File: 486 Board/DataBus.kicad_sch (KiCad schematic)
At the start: 16 parts, among them U21 74245, U22 74245, U23 74245, U24 74245, U25 74245, U26 74245, U27 74245, U28 74245

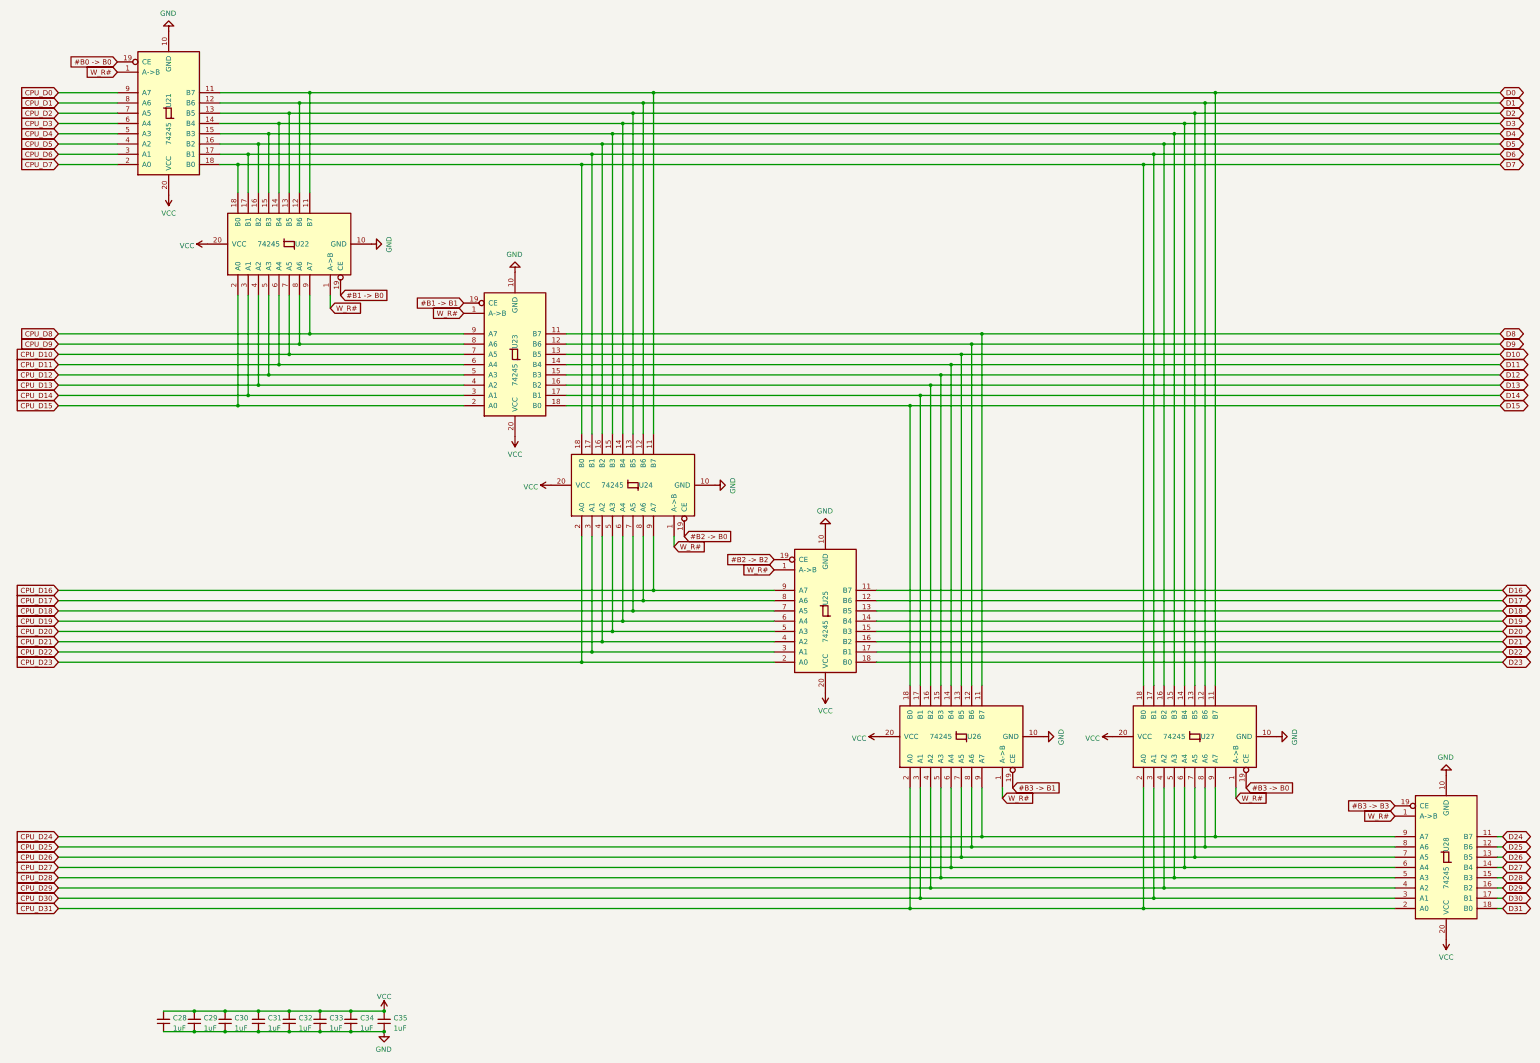
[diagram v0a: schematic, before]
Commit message: * Layout Template for eurocard format * 486 Board updated to new layout * Support board draft * Added 6u eurocard backplane meant for ATX case
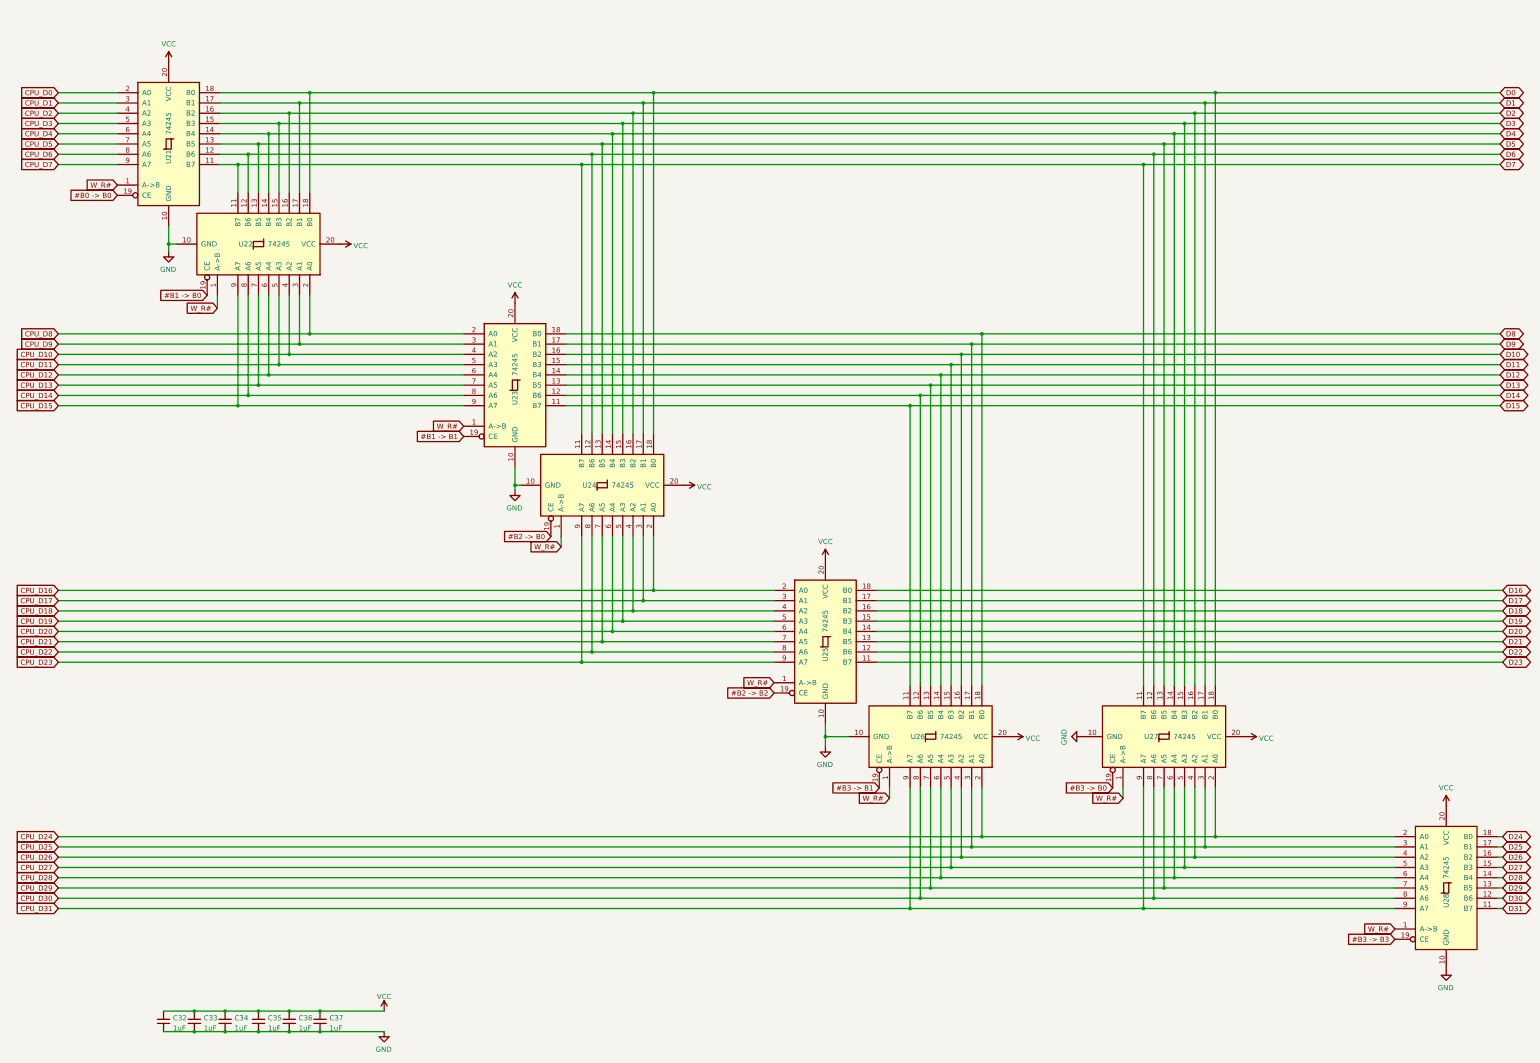
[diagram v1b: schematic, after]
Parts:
- removed C34, C35: 1uF, Capacitor_SMD:C_0805_2012Metric_Pad1.18x1.45mm_HandSolder, symbol Device:C_Small
- renumbered C28 to C32, C29 to C33, C30 to C34, C31 to C35, C32 to C36, C33 to C37
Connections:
- net CPU_D0: now also U21.2 (A0); no longer U21.9 (A7)
- net CPU_D1: now also U21.3 (A1); no longer U21.8 (A6)
- net CPU_D10: now also U22.4 (A2), U23.4 (A2); no longer U22.7 (A5), U23.7 (A5)
- net CPU_D11: now also U22.5 (A3), U23.5 (A3); no longer U22.6 (A4), U23.6 (A4)
- net CPU_D12: now also U22.6 (A4), U23.6 (A4); no longer U22.5 (A3), U23.5 (A3)
- net CPU_D13: now also U22.7 (A5), U23.7 (A5); no longer U22.4 (A2), U23.4 (A2)
- net CPU_D14: now also U22.8 (A6), U23.8 (A6); no longer U22.3 (A1), U23.3 (A1)
- net CPU_D15: now also U22.9 (A7), U23.9 (A7); no longer U22.2 (A0), U23.2 (A0)
- net CPU_D16: now also U24.2 (A0), U25.2 (A0); no longer U24.9 (A7), U25.9 (A7)
- net CPU_D17: now also U24.3 (A1), U25.3 (A1); no longer U24.8 (A6), U25.8 (A6)
- net CPU_D18: now also U24.4 (A2), U25.4 (A2); no longer U24.7 (A5), U25.7 (A5)
- net CPU_D19: now also U24.5 (A3), U25.5 (A3); no longer U24.6 (A4), U25.6 (A4)
- net CPU_D2: now also U21.4 (A2); no longer U21.7 (A5)
- net CPU_D20: now also U24.6 (A4), U25.6 (A4); no longer U24.5 (A3), U25.5 (A3)
- net CPU_D21: now also U24.7 (A5), U25.7 (A5); no longer U24.4 (A2), U25.4 (A2)
- net CPU_D22: now also U24.8 (A6), U25.8 (A6); no longer U24.3 (A1), U25.3 (A1)
- net CPU_D23: now also U24.9 (A7), U25.9 (A7); no longer U24.2 (A0), U25.2 (A0)
- net CPU_D24: now also U26.2 (A0), U27.2 (A0), U28.2 (A0); no longer U26.9 (A7), U27.9 (A7), U28.9 (A7)
- net CPU_D25: now also U26.3 (A1), U27.3 (A1), U28.3 (A1); no longer U26.8 (A6), U27.8 (A6), U28.8 (A6)
- net CPU_D26: now also U26.4 (A2), U27.4 (A2), U28.4 (A2); no longer U26.7 (A5), U27.7 (A5), U28.7 (A5)
- net CPU_D27: now also U26.5 (A3), U27.5 (A3), U28.5 (A3); no longer U26.6 (A4), U27.6 (A4), U28.6 (A4)
- net CPU_D28: now also U26.6 (A4), U27.6 (A4), U28.6 (A4); no longer U26.5 (A3), U27.5 (A3), U28.5 (A3)
- net CPU_D29: now also U26.7 (A5), U27.7 (A5), U28.7 (A5); no longer U26.4 (A2), U27.4 (A2), U28.4 (A2)
- net CPU_D3: now also U21.5 (A3); no longer U21.6 (A4)
- net CPU_D30: now also U26.8 (A6), U27.8 (A6), U28.8 (A6); no longer U26.3 (A1), U27.3 (A1), U28.3 (A1)
- net CPU_D31: now also U26.9 (A7), U27.9 (A7), U28.9 (A7); no longer U26.2 (A0), U27.2 (A0), U28.2 (A0)
- net CPU_D4: now also U21.6 (A4); no longer U21.5 (A3)
- net CPU_D5: now also U21.7 (A5); no longer U21.4 (A2)
- net CPU_D6: now also U21.8 (A6); no longer U21.3 (A1)
- net CPU_D7: now also U21.9 (A7); no longer U21.2 (A0)
- net CPU_D8: now also U22.2 (A0), U23.2 (A0); no longer U22.9 (A7), U23.9 (A7)
- net CPU_D9: now also U22.3 (A1), U23.3 (A1); no longer U22.8 (A6), U23.8 (A6)
- net D0: now also U21.18 (B0), U22.18 (B0), U24.18 (B0), U27.18 (B0); no longer U21.11 (B7), U22.11 (B7), U24.11 (B7), U27.11 (B7)
- net D1: now also U21.17 (B1), U22.17 (B1), U24.17 (B1), U27.17 (B1); no longer U21.12 (B6), U22.12 (B6), U24.12 (B6), U27.12 (B6)
- net D10: now also U23.16 (B2), U26.16 (B2); no longer U23.13 (B5), U26.13 (B5)
- net D11: now also U23.15 (B3), U26.15 (B3); no longer U23.14 (B4), U26.14 (B4)
- net D12: now also U23.14 (B4), U26.14 (B4); no longer U23.15 (B3), U26.15 (B3)
- net D13: now also U23.13 (B5), U26.13 (B5); no longer U23.16 (B2), U26.16 (B2)
- net D14: now also U23.12 (B6), U26.12 (B6); no longer U23.17 (B1), U26.17 (B1)
- net D15: now also U23.11 (B7), U26.11 (B7); no longer U23.18 (B0), U26.18 (B0)
- net D16: now also U25.18 (B0); no longer U25.11 (B7)
- net D17: now also U25.17 (B1); no longer U25.12 (B6)
- net D18: now also U25.16 (B2); no longer U25.13 (B5)
- net D19: now also U25.15 (B3); no longer U25.14 (B4)
- net D2: now also U21.16 (B2), U22.16 (B2), U24.16 (B2), U27.16 (B2); no longer U21.13 (B5), U22.13 (B5), U24.13 (B5), U27.13 (B5)
- net D20: now also U25.14 (B4); no longer U25.15 (B3)
- net D21: now also U25.13 (B5); no longer U25.16 (B2)
- net D22: now also U25.12 (B6); no longer U25.17 (B1)
- net D23: now also U25.11 (B7); no longer U25.18 (B0)
- net D24: now also U28.18 (B0); no longer U28.11 (B7)
- net D25: now also U28.17 (B1); no longer U28.12 (B6)
- net D26: now also U28.16 (B2); no longer U28.13 (B5)
- net D27: now also U28.15 (B3); no longer U28.14 (B4)
- net D28: now also U28.14 (B4); no longer U28.15 (B3)
- net D29: now also U28.13 (B5); no longer U28.16 (B2)
- net D3: now also U21.15 (B3), U22.15 (B3), U24.15 (B3), U27.15 (B3); no longer U21.14 (B4), U22.14 (B4), U24.14 (B4), U27.14 (B4)
- net D30: now also U28.12 (B6); no longer U28.17 (B1)
- net D31: now also U28.11 (B7); no longer U28.18 (B0)
- net D4: now also U21.14 (B4), U22.14 (B4), U24.14 (B4), U27.14 (B4); no longer U21.15 (B3), U22.15 (B3), U24.15 (B3), U27.15 (B3)
- net D5: now also U21.13 (B5), U22.13 (B5), U24.13 (B5), U27.13 (B5); no longer U21.16 (B2), U22.16 (B2), U24.16 (B2), U27.16 (B2)
- net D6: now also U21.12 (B6), U22.12 (B6), U24.12 (B6), U27.12 (B6); no longer U21.17 (B1), U22.17 (B1), U24.17 (B1), U27.17 (B1)
- net D7: now also U21.11 (B7), U22.11 (B7), U24.11 (B7), U27.11 (B7); no longer U21.18 (B0), U22.18 (B0), U24.18 (B0), U27.18 (B0)
- net D8: now also U23.18 (B0), U26.18 (B0); no longer U23.11 (B7), U26.11 (B7)
- net D9: now also U23.17 (B1), U26.17 (B1); no longer U23.12 (B6), U26.12 (B6)
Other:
- moved on the sheet: U21, U22, U23, U24, U25, U26, U27, U28
